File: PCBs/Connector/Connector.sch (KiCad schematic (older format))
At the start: 3 parts, among them J1 MCU, J2 Accel, J3 Charger

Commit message: Changed
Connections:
- net labels removed: AC_CS
- wire segments 41 -> 38
- no-connect marks 3 -> 2
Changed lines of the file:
@@
 LIBS:audio
 LIBS:interface
+LIBS:Connector-cache
 EELAYER 26 0
 EELAYER END
@@
 	5100 4800 5200 4800
 Wire Wire Line
-	5100 4800 5100 3600
-Wire Wire Line
 	5100 3600 5200 3600
 Connection ~ 5100 4800
@@
 Text Label 4900 3500 0    50   ~ 0
 VBAT
-Text Label 4700 3100 0    50   ~ 0
-SCL
-Text Label 4700 3000 0    50   ~ 0
-SDA
-Text Label 4700 2800 0    50   ~ 0
-AC_INT1
-Text Label 4700 2900 0    50   ~ 0
-AC_INT2
-Text Label 4700 2700 0    50   ~ 0
-AC_CS
-Text Label 4700 2600 0    50   ~ 0
-QSTRT
-Text Label 4700 2500 0    50   ~ 0
-~ALRT
-Text Label 4700 2400 0    50   ~ 0
-~STAT
 Wire Wire Line
 	5200 5400 4900 5400
@@
 	5200 4700 4700 4700
 Connection ~ 4700 4700
-Wire Wire Line
-	4700 4700 4700 3400
 NoConn ~ 5200 3200
 NoConn ~ 5200 3300
-NoConn ~ 5200 4300
 Wire Wire Line
 	5200 5600 3900 5600
 Wire Wire Line
-	3900 5600 3900 4200
-Wire Wire Line
-	5200 4200 3900 4200
+	5200 4200 4300 4200
 Wire Wire Line
 	5200 5700 3700 5700
 Wire Wire Line
-	3700 5700 3700 4100
-Wire Wire Line
-	5200 4100 3700 4100
-Wire Wire Line
 	5200 5800 3500 5800
-Wire Wire Line
-	3500 5800 3500 2600
 Wire Wire Line
 	3500 2600 5200 2600
@@
 	5200 5900 3300 5900
 Wire Wire Line
-	3300 5900 3300 2500
-Wire Wire Line
 	3300 2500 5200 2500
 Wire Wire Line
 	5200 6000 3100 6000
-Wire Wire Line
-	3100 6000 3100 2400
-Wire Wire Line
-	3100 2400 5200 2400
 $Comp
 L Connector_Generic:Conn_01x13 J1
@@
 $EndComp
 Wire Wire Line
-	5200 4600 4100 4600
+	5200 4300 4700 4300
+Connection ~ 4700 4300
 Wire Wire Line
-	5200 4500 4300 4500
+	4700 4300 4700 3400
+Text Label 4700 3000 0    50   ~ 0
+AC_INT1
+Text Label 4700 3100 0    50   ~ 0
+AC_INT2
+Text Label 4700 2800 0    50   ~ 0
+QSTRT
+Text Label 4700 2600 0    50   ~ 0
+~ALRT
+Text Label 4700 2900 0    50   ~ 0
+~STAT
+Text Label 4700 2700 0    50   ~ 0
+SCL
+Text Label 4700 2400 0    50   ~ 0
+SDA
 Wire Wire Line
-	5200 4400 4500 4400
+	4700 4300 4700 4600
 Wire Wire Line
-	3900 4200 3900 3000
+	5100 3600 5100 4800
+Wire Wire Line
+	5200 4600 4700 4600
+Connection ~ 4700 4600
+Wire Wire Line
+	4700 4600 4700 4700
+Wire Wire Line
+	5200 4100 4500 4100
+Wire Wire Line
+	4500 4100 4500 2700
+Wire Wire Line
+	4500 2700 5200 2700
+Wire Wire Line
+	3700 2900 5200 2900
+Wire Wire Line
+	3700 2800 5200 2800
+Wire Wire Line
+	4300 4200 4300 2400
+Wire Wire Line
+	4300 2400 5200 2400
+Wire Wire Line
+	5200 4400 4100 4400
+Wire Wire Line
+	4100 4400 4100 3100
+Wire Wire Line
+	4100 3100 5200 3100
+Wire Wire Line
+	5200 4500 3900 4500
+Wire Wire Line
+	3900 4500 3900 3000
 Wire Wire Line
 	3900 3000 5200 3000
-Connection ~ 3900 4200
-Wire Wire Line
-	3700 4100 3700 3100
-Wire Wire Line
-	3700 3100 5200 3100
-Connection ~ 3700 4100
-Wire Wire Line
-	4500 4400 4500 2900
-Wire Wire Line
-	4500 2900 5200 2900
-Wire Wire Line
-	4300 4500 4300 2800
-Wire Wire Line
-	4300 2800 5200 2800
-Wire Wire Line
-	4100 4600 4100 2700
-Wire Wire Line
-	4100 2700 5200 2700
 $EndSCHEMATC

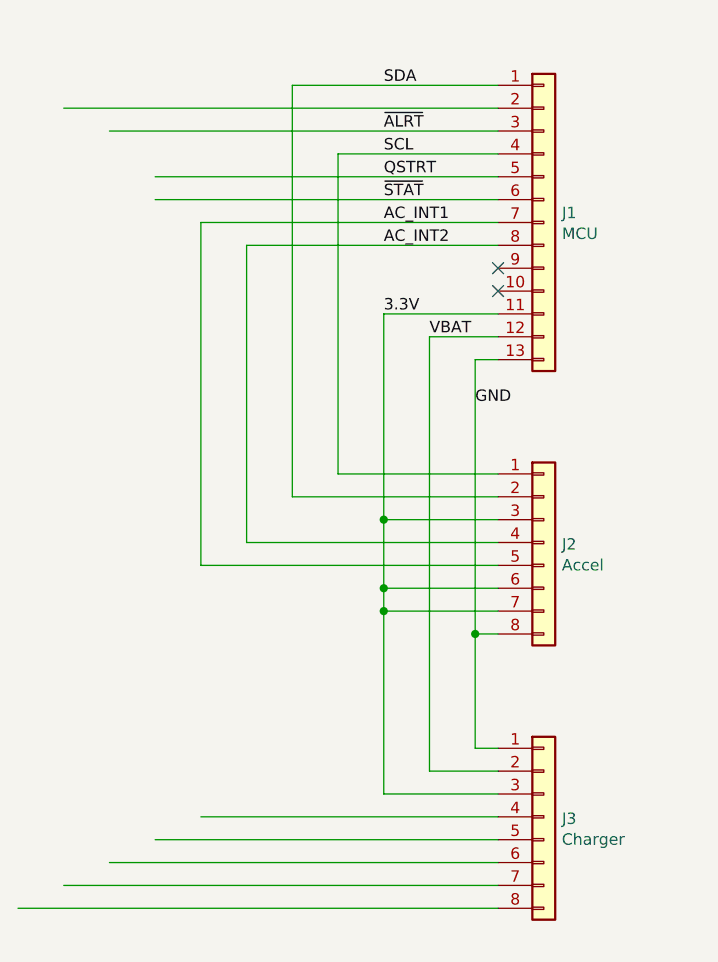
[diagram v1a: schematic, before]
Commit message: Fixed some output pins.
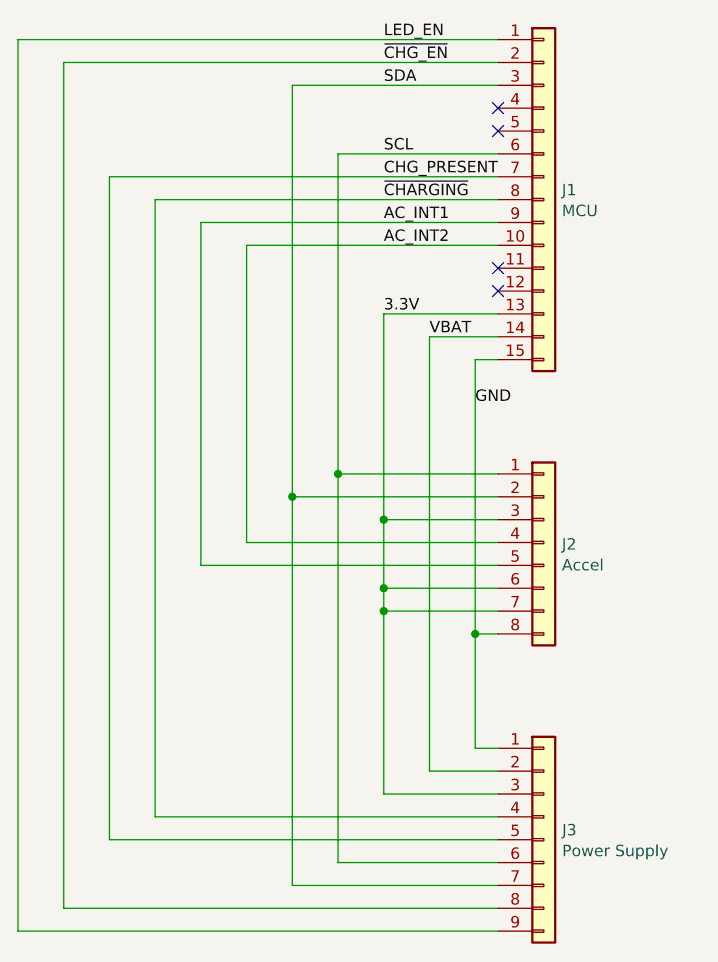
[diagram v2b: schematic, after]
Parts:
- removed J1: MCU, Pin_Headers:Pin_Header_Straight_1x13_Pitch2.54mm, symbol Connector_Generic:Conn_01x13
- removed J3: Charger, Pin_Headers:Pin_Header_Straight_1x08_Pitch2.54mm, symbol Connector_Generic:Conn_01x08
- added J1: MCU, symbol Connector_Generic:Conn_01x15
- added J3: Power Supply, symbol Connector_Generic:Conn_01x09
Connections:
- net labels added: CHG_PRESENT, LED_EN, ~CHARGING, ~CHG_EN
- net labels removed: QSTRT, ~ALRT, ~STAT
- wire segments 38 -> 45
- no-connect marks 2 -> 4
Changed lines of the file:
@@
 $EndDescr
-$Comp
-L Connector_Generic:Conn_01x08 J3
-U 1 1 5DBA26D9
-P 5400 5600
-F 0 "J3" H 5479 5592 50  0000 L CNN
-F 1 "Charger" H 5479 5501 50  0000 L CNN
-F 2 "Pin_Headers:Pin_Header_Straight_1x08_Pitch2.54mm" H 5400 5600 50  0001 C CNN
-F 3 "~" H 5400 5600 50  0001 C CNN
-	1    5400 5600
-	1    0    0    -1
-$EndComp
 $Comp
 L Connector_Generic:Conn_01x08 J2
@@
 NoConn ~ 5200 3300
 Wire Wire Line
-	5200 5600 3900 5600
-Wire Wire Line
 	5200 4200 4300 4200
-Wire Wire Line
-	5200 5700 3700 5700
-Wire Wire Line
-	5200 5800 3500 5800
-Wire Wire Line
-	3500 2600 5200 2600
-Wire Wire Line
-	5200 5900 3300 5900
-Wire Wire Line
-	3300 2500 5200 2500
-Wire Wire Line
-	5200 6000 3100 6000
-$Comp
-L Connector_Generic:Conn_01x13 J1
-U 1 1 5DBA70D7
-P 5400 3000
-F 0 "J1" H 5479 3042 50  0000 L CNN
-F 1 "MCU" H 5479 2951 50  0000 L CNN
-F 2 "Pin_Headers:Pin_Header_Straight_1x13_Pitch2.54mm" H 5400 3000 50  0001 C CNN
-F 3 "~" H 5400 3000 50  0001 C CNN
-	1    5400 3000
-	1    0    0    -1
-$EndComp
 Wire Wire Line
 	5200 4300 4700 4300
@@
 AC_INT2
 Text Label 4700 2800 0    50   ~ 0
-QSTRT
-Text Label 4700 2600 0    50   ~ 0
-~ALRT
+CHG_PRESENT
+Text Label 4700 2300 0    50   ~ 0
+~CHG_EN
 Text Label 4700 2900 0    50   ~ 0
-~STAT
+~CHARGING
 Text Label 4700 2700 0    50   ~ 0
 SCL
@@
 	3700 2900 5200 2900
 Wire Wire Line
-	3700 2800 5200 2800
-Wire Wire Line
 	4300 4200 4300 2400
 Wire Wire Line
@@
 Wire Wire Line
 	3900 3000 5200 3000
+Text Label 4700 2200 0    50   ~ 0
+LED_EN
+Wire Wire Line
+	3700 5600 3700 2900
+Wire Wire Line
+	3700 5600 5200 5600
+Wire Wire Line
+	3500 2800 3500 5700
+Wire Wire Line
+	3500 5700 5200 5700
+Wire Wire Line
+	3500 2800 5200 2800
+Wire Wire Line
+	4500 4100 4500 5800
+Connection ~ 4500 4100
+Wire Wire Line
+	4500 5800 5200 5800
+$Comp
+L Connector_Generic:Conn_01x09 J3
+U 1 1 5DC12E08
+P 5400 5700
+F 0 "J3" H 5480 5742 50  0000 L CNN
+F 1 "Power Supply" H 5480 5651 50  0000 L CNN
+F 2 "" H 5400 5700 50  0001 C CNN
+F 3 "~" H 5400 5700 50  0001 C CNN
+	1    5400 5700
+	1    0    0    -1
+$EndComp
+Wire Wire Line
+	4300 4200 4300 5900
+Connection ~ 4300 4200
+$Comp
+L Connector_Generic:Conn_01x15 J1
+U 1 1 5DC13B06
+P 5400 2900
+F 0 "J1" H 5479 2942 50  0000 L CNN
+F 1 "MCU" H 5479 2851 50  0000 L CNN
+F 2 "" H 5400 2900 50  0001 C CNN
+F 3 "~" H 5400 2900 50  0001 C CNN
+	1    5400 2900
+	1    0    0    -1
+$EndComp
+Wire Wire Line
+	3100 2200 5200 2200
+Wire Wire Line
+	3300 2300 5200 2300
+Wire Wire Line
+	5200 5900 4300 5900
+Wire Wire Line
+	3300 6000 5200 6000
+Wire Wire Line
+	3300 2300 3300 6000
+Wire Wire Line
+	3100 6100 5200 6100
+Wire Wire Line
+	3100 2200 3100 6100
+NoConn ~ 5200 2500
+NoConn ~ 5200 2600
 $EndSCHEMATC

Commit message: New designs
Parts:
- removed J3: Power Supply, symbol Connector_Generic:Conn_01x09
- added J3: Power Supply, Pin_Headers:Pin_Header_Straight_1x08_Pitch2.54mm, symbol Connector_Generic:Conn_01x08
- J1: footprint (none) -> Pin_Headers:Pin_Header_Straight_1x15_Pitch2.54mm
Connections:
- net CHG_PRESENT: now also J3.4 (Pin_4)
- net GND: now also J3.1 (Pin_1)
- net LED_EN: now also J3.8 (Pin_8)
- net SCL: now also J3.5 (Pin_5)
- net SDA: now also J3.6 (Pin_6)
- net VBAT: now also J3.2 (Pin_2)
- net ~CHARGING: now also J3.3 (Pin_3)
- net ~CHG_EN: now also J3.7 (Pin_7)
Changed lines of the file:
@@
 	4900 3500 5200 3500
-Wire Wire Line
-	5200 5500 4700 5500
-Wire Wire Line
-	4700 5500 4700 4700
 Wire Wire Line
 	4700 3400 5200 3400
 Wire Wire Line
 	5200 4700 4700 4700
-Connection ~ 4700 4700
 NoConn ~ 5200 3200
 NoConn ~ 5200 3300
@@
 LED_EN
 Wire Wire Line
-	3700 5600 3700 2900
-Wire Wire Line
-	3700 5600 5200 5600
-Wire Wire Line
-	3500 2800 3500 5700
-Wire Wire Line
-	3500 5700 5200 5700
+	3500 2800 3500 5600
 Wire Wire Line
 	3500 2800 5200 2800
 Wire Wire Line
-	4500 4100 4500 5800
+	4500 4100 4500 5700
 Connection ~ 4500 4100
 Wire Wire Line
-	4500 5800 5200 5800
-$Comp
-L Connector_Generic:Conn_01x09 J3
-U 1 1 5DC12E08
-P 5400 5700
-F 0 "J3" H 5480 5742 50  0000 L CNN
-F 1 "Power Supply" H 5480 5651 50  0000 L CNN
-F 2 "" H 5400 5700 50  0001 C CNN
-F 3 "~" H 5400 5700 50  0001 C CNN
-	1    5400 5700
-	1    0    0    -1
-$EndComp
-Wire Wire Line
-	4300 4200 4300 5900
+	4300 4200 4300 5800
 Connection ~ 4300 4200
 $Comp
@@
 F 0 "J1" H 5479 2942 50  0000 L CNN
 F 1 "MCU" H 5479 2851 50  0000 L CNN
-F 2 "" H 5400 2900 50  0001 C CNN
+F 2 "Pin_Headers:Pin_Header_Straight_1x15_Pitch2.54mm" H 5400 2900 50  0001 C CNN
 F 3 "~" H 5400 2900 50  0001 C CNN
 	1    5400 2900
@@
 	3300 2300 5200 2300
 Wire Wire Line
-	5200 5900 4300 5900
+	3300 2300 3300 5900
 Wire Wire Line
-	3300 6000 5200 6000
-Wire Wire Line
-	3300 2300 3300 6000
-Wire Wire Line
-	3100 6100 5200 6100
-Wire Wire Line
-	3100 2200 3100 6100
+	3100 2200 3100 6000
 NoConn ~ 5200 2500
 NoConn ~ 5200 2600
+$Comp
+L Connector_Generic:Conn_01x08 J3
+U 1 1 5DC1B29E
+P 5400 5600
+F 0 "J3" H 5479 5592 50  0000 L CNN
+F 1 "Power Supply" H 5479 5501 50  0000 L CNN
+F 2 "Pin_Headers:Pin_Header_Straight_1x08_Pitch2.54mm" H 5400 5600 50  0001 C CNN
+F 3 "~" H 5400 5600 50  0001 C CNN
+	1    5400 5600
+	1    0    0    -1
+$EndComp
+Wire Wire Line
+	5200 5500 3700 5500
+Wire Wire Line
+	3700 5500 3700 2900
+Wire Wire Line
+	5200 5600 3500 5600
+Wire Wire Line
+	5200 5700 4500 5700
+Wire Wire Line
+	5200 5800 4300 5800
+Wire Wire Line
+	5200 5900 3300 5900
+Wire Wire Line
+	5200 6000 3100 6000
 $EndSCHEMATC
